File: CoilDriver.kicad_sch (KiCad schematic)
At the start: 27 parts, among them Q8 IRLML2803, Q9 SiRA99DP, U7 DRV8235RTER

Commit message: v3.1 Updates
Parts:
- removed Q9: SiRA99DP, Argus-Miscellaneous:PowerPAK SO-8, symbol Argus-IC:Q_PMOS_GDS
- removed R28, R30: 0R, Resistor_SMD:R_0603_1608Metric, symbol Device:R_Small
- added Q23: SIRA99DP-T1-GE3, Package_SO:PowerPAK_SO-8_Single, symbol Transistor_FET:Si7141DP
- C26: renamed from C11; value 10uF -> 10u; symbol Device:C -> Device:C_Small; MPN (none) -> C126617
- C27: renamed from C12; value 0.1uF -> 100n; symbol Device:C -> Device:C_Small; MPN (none) -> C307348
- C28: renamed from C13; value 1nF -> 1n; symbol Device:C -> Device:C_Small; MPN (none) -> C161231
- C29: renamed from C14; value 0.1uF -> 100n; symbol Device:C -> Device:C_Small; MPN (none) -> C307348
- D8: renamed from D3; DIS Digi-Key -> (none); DPN 1830-1064-1-ND -> (none); MFR Inolux -> (none); MPN IN-S63AT5A -> C2909774
- D9: renamed from D4; value 10V -> PTVS10VZ1USK; Field5 (none) -> 10V
- Q22: renamed from Q8; MPN (none) -> C2590
- R80: renamed from R19; value 2.7k -> 2k7; DIS Digi-Key -> (none); DPN A129693CT-ND -> (none); MFR TE -> (none); MPN CRGCQ0603F2K7 -> C237112
- R81: renamed from R22; DIS Digi-Key -> (none); DPN 311-10.0KHRCT-ND -> (none); MFR Yageo -> (none); MPN RC0603FR-0710KL -> C2479067
- R82: renamed from R23; MPN (none) -> C844931
- R83: renamed from R24; DIS Digi-Key -> (none); DPN 311-10.0KHRCT-ND -> (none); MFR Yageo -> (none); MPN RC0603FR-0710KL -> C2479067
- R84: renamed from R27; symbol Device:R -> Device:R_Small; MPN (none) -> C2479067
- R85: renamed from R33; MPN (none) -> C2484712
- R86: renamed from R29; MPN (none) -> C844915
- R87: renamed from R31; MPN (none) -> C844915
- R88: renamed from R20; MPN (none) -> C844915
- R89: renamed from R21; DNI (none) -> DNI; now not fitted; now left out of the parts list
- R90: renamed from R25; DNI (none) -> DNI; now not fitted; now left out of the parts list
- R91: renamed from R26; MPN (none) -> C844915
- R92: renamed from R32; symbol Device:R -> Device:R_Small
- R93: renamed from R34; symbol Device:R -> Device:R_Small
- R94: renamed from R35; symbol Device:R -> Device:R_Small
- renumbered F6 to F9, U7 to U8
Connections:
- net VM: now also Q23.5 (D)
- net at Q22.3 (D), R83.1: now also Q23.4 (G)
- net at F9.1, R83.2: now also Q23.1 (S), Q23.2 (S), Q23.3 (S)
- net A0_COIL renamed A0
- net A1_COIL renamed A1
- net MAIN_3V3 renamed 3V3_P
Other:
- sheet I2C Single Protection1 renamed I2C Single Protection10
- sheet I2C Single Protection2 renamed I2C Single Protection11
- note added: "#TODO: Spec Resistors"
- note added: "I2C ADDR R86, R87 +Z: 0R, 0R: 0x30 Translated: 0x10"
- company: (none) -> Carnegie Mellon University
- title: (none) -> Argus +Z Solar Panel
- moved on the sheet: C26, C27, C28, C29, D8, D9, F9, Q22, R80, R81, R82, R83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

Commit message: Local Stash
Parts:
- R87: now not fitted; now left out of the parts list
- R92: value TBD -> 560R
- R93: value TBD -> 2k7
- R94: value TBD -> 1M
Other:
- note added: "I2C ADDR R86, R87 +Z: 0R, DNP: 0x33"
- note removed: "I2C ADDR R86, R87 +Z: 0R, 0R: 0x30 Translated: 0x10"
- moved on the sheet: C29, R93, R94
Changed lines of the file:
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@@
 		)
 	)
-	(text "I2C ADDR\nR86, R87\n+Z: 0R, 0R: 0x30\nTranslated: 0x10"
+	(text "I2C ADDR\nR86, R87\n+Z: 0R, DNP: 0x33"
 		(exclude_from_sim no)
 		(at 144.526 117.856 0)
@@
 	(text "Populate after\nsetting VM\n\nStall Current = \nVREF/(R*0.0015)"
 		(exclude_from_sim no)
-		(at 182.372 144.78 0)
+		(at 182.372 144.018 0)
 		(effects
 			(font
@@
 	)
 	(junction
-		(at 226.06 135.89)
+		(at 226.06 138.43)
 		(diameter 0)
 		(color 0 0 0 0)
@@
 	(wire
 		(pts
-			(xy 209.55 135.89) (xy 209.55 138.43)
+			(xy 209.55 138.43) (xy 209.55 140.97)
 		)
 		(stroke
@@
 	(wire
 		(pts
-			(xy 226.06 133.35) (xy 226.06 135.89)
+			(xy 226.06 135.89) (xy 226.06 138.43)
 		)
 		(stroke
@@
 	(wire
 		(pts
-			(xy 226.06 135.89) (xy 240.03 135.89)
+			(xy 226.06 138.43) (xy 240.03 138.43)
 		)
 		(stroke
@@
 	(wire
 		(pts
-			(xy 209.55 143.51) (xy 209.55 146.05)
+			(xy 209.55 146.05) (xy 209.55 148.59)
 		)
 		(stroke
@@
 	(wire
 		(pts
-			(xy 209.55 135.89) (xy 226.06 135.89)
+			(xy 209.55 138.43) (xy 226.06 138.43)
 		)
 		(stroke
@@
 	(wire
 		(pts
-			(xy 226.06 135.89) (xy 226.06 138.43)
+			(xy 226.06 138.43) (xy 226.06 140.97)
 		)
 		(stroke
@@
 	(wire
 		(pts
-			(xy 226.06 143.51) (xy 226.06 146.05)
+			(xy 226.06 146.05) (xy 226.06 148.59)
 		)
 		(stroke
@@
 	(wire
 		(pts
-			(xy 226.06 125.73) (xy 226.06 128.27)
+			(xy 226.06 128.27) (xy 226.06 130.81)
 		)
 		(stroke
@@
 	)
 	(label "VREF"
-		(at 240.03 135.89 180)
+		(at 240.03 138.43 180)
 		(effects
 			(font
@@
 	(symbol
 		(lib_id "Device:R_Small")
-		(at 226.06 130.81 0)
+		(at 226.06 133.35 0)
 		(unit 1)
 		(exclude_from_sim no)
@@
 		(dnp no)
 		(property "Reference" "R93"
-			(at 227.584 129.794 0)
+			(at 227.33 132.334 0)
 			(effects
 				(font
@@
 			)
 		)
-		(property "Value" "TBD"
-			(at 227.584 132.08 0)
+		(property "Value" "2k7"
+			(at 227.33 134.62 0)
 			(effects
 				(font
@@
 		)
 		(property "Footprint" "Resistor_SMD:R_0603_1608Metric"
-			(at 226.06 130.81 0)
+			(at 226.06 133.35 0)
 			(effects
 				(font
@@
 		)
 		(property "Datasheet" "~"
-			(at 226.06 130.81 0)
+			(at 226.06 133.35 0)
 			(effects
 				(font
@@
 		)
 		(property "Description" "Resistor, small symbol"
-			(at 226.06 130.81 0)
+			(at 226.06 133.35 0)
 			(effects
 				(font
@@
 	(symbol
 		(lib_id "Device:C_Small")
-		(at 209.55 140.97 0)
+		(at 209.55 143.51 0)
 		(unit 1)
 		(exclude_from_sim no)
@@
 		(dnp no)
 		(property "Reference" "C29"
-			(at 211.836 139.954 0)
+			(at 211.836 142.494 0)
 			(effects
 				(font
@@
 		)
 		(property "Value" "100n"
-			(at 211.836 141.986 0)
+			(at 211.836 144.526 0)
 			(effects
 				(font
@@
 		)
 		(property "Footprint" "Capacitor_SMD:C_0603_1608Metric"
-			(at 209.55 140.97 0)
+			(at 209.55 143.51 0)
 			(effects
 				(font
@@
 		)
 		(property "Datasheet" "~"
-			(at 209.55 140.97 0)
+			(at 209.55 143.51 0)
 			(effects
 				(font
@@
 		)
 		(property "Description" "Unpolarized capacitor, small symbol"
-			(at 209.55 140.97 0)
+			(at 209.55 143.51 0)
 			(effects
 				(font
@@
 		)
 		(property "MPN" "C307348"
-			(at 209.55 140.97 0)
+			(at 209.55 143.51 0)
 			(effects
 				(font
@@
 	(symbol
 		(lib_id "power:GND")
-		(at 209.55 146.05 0)
+		(at 209.55 148.59 0)
 		(unit 1)
 		(exclude_from_sim no)
@@
 		(on_board yes)
 		(dnp no)
-		(fields_autoplaced yes)
 		(property "Reference" "#PWR035"
-			(at 209.55 152.4 0)
+			(at 209.55 154.94 0)
 			(effects
 				(font
@@
 		)
 		(property "Value" "GND"
-			(at 209.55 151.13 0)
+			(at 209.55 152.4 0)
 			(effects
 				(font
@@
 		)
 		(property "Footprint" ""
-			(at 209.55 146.05 0)
+			(at 209.55 148.59 0)
 			(effects
 				(font
@@
 		)
 		(property "Datasheet" ""
-			(at 209.55 146.05 0)
+			(at 209.55 148.59 0)
 			(effects
 				(font
@@
 		)
 		(property "Description" "Power symbol creates a global label with name \"GND\" , ground"
-			(at 209.55 146.05 0)
+			(at 209.55 148.59 0)
 			(effects
 				(font
@@
 	(symbol
 		(lib_id "power:GND")
-		(at 226.06 146.05 0)
+		(at 226.06 148.59 0)
 		(unit 1)
 		(exclude_from_sim no)
@@
 		(on_board yes)
 		(dnp no)
-		(fields_autoplaced yes)
 		(property "Reference" "#PWR037"
-			(at 226.06 152.4 0)
+			(at 226.06 154.94 0)
 			(effects
 				(font
@@
 		)
 		(property "Value" "GND"
-			(at 226.06 151.13 0)
+			(at 226.06 152.4 0)
 			(effects
 				(font
@@
 		)
 		(property "Footprint" ""
-			(at 226.06 146.05 0)
+			(at 226.06 148.59 0)
 			(effects
 				(font
@@
 		)
 		(property "Datasheet" ""
-			(at 226.06 146.05 0)
+			(at 226.06 148.59 0)
 			(effects
 				(font
@@
 		)
 		(property "Description" "Power symbol creates a global label with name \"GND\" , ground"
-			(at 226.06 146.05 0)
+			(at 226.06 148.59 0)
 			(effects
 				(font
@@
 	(symbol
 		(lib_id "power:+3.3V")
-		(at 226.06 125.73 0)
+		(at 226.06 128.27 0)
 		(mirror y)
 		(unit 1)
@@
 		(dnp no)
 		(property "Reference" "#SUPPLY07"
-			(at 226.06 125.73 0)
+			(at 226.06 128.27 0)
 			(effects
 				(font
@@
 		)
 		(property "Value" "3V3_P"
-			(at 226.06 121.92 0)
+			(at 226.06 124.46 0)
 			(effects
 				(font
@@
 		)
 		(property "Footprint" ""
-			(at 226.06 125.73 0)
+			(at 226.06 128.27 0)
 			(effects
 				(font
@@
 		)
 		(property "Datasheet" ""
-			(at 226.06 125.73 0)
+			(at 226.06 128.27 0)
 			(effects
 				(font
@@
 		)
 		(property "Description" "Power symbol creates a global label with name \"+3.3V\""
-			(at 226.06 125.73 0)
+			(at 226.06 128.27 0)
 			(effects
 				(font
@@
 			)
 		)
-		(property "Value" "TBD"
+		(property "Value" "560R"
 			(at 164.084 141.986 0)
 			(effects
@@
 	(symbol
 		(lib_id "Device:R_Small")
-		(at 226.06 140.97 0)
+		(at 226.06 143.51 0)
 		(unit 1)
 		(exclude_from_sim no)
@@
 		(dnp no)
 		(property "Reference" "R94"
-			(at 227.33 139.954 0)
+			(at 227.33 142.494 0)
 			(effects
 				(font
@@
 			)
 		)
-		(property "Value" "TBD"
-			(at 227.33 142.24 0)
+		(property "Value" "1M"
+			(at 227.33 144.78 0)
 			(effects
 				(font
@@
 		)
 		(property "Footprint" "Resistor_SMD:R_0603_1608Metric"
-			(at 226.06 140.97 0)
+			(at 226.06 143.51 0)
 			(effects
 				(font
@@
 		)
 		(property "Datasheet" "~"
-			(at 226.06 140.97 0)
+			(at 226.06 143.51 0)
 			(effects
 				(font
@@
 		)
 		(property "Description" "Resistor, small symbol"
-			(at 226.06 140.97 0)
+			(at 226.06 143.51 0)
 			(effects
 				(font
@@
 		(unit 1)
 		(exclude_from_sim no)
-		(in_bom yes)
+		(in_bom no)
 		(on_board yes)
-		(dnp no)
+		(dnp yes)
 		(property "Reference" "R87"
 			(at 196.342 109.728 0)

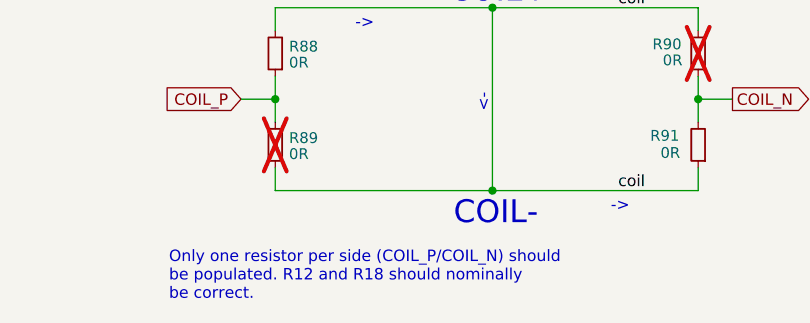
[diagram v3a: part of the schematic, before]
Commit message: Coil direction comment clarification
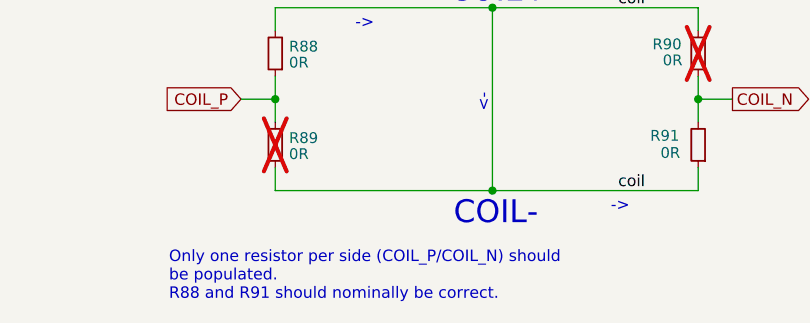
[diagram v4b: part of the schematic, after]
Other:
- note added: "Only one resistor per side (COIL_P/COIL_N) should be populated. R88 and R91 should nominally be correct."
- note removed: "Only one resistor per side (COIL_P/COIL_N) should be populated. R12 and R18 should nominally be correct."
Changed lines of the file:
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@@
 		)
 	)
-	(text "Only one resistor per side (COIL_P/COIL_N) should \nbe populated. R12 and R18 should nominally \nbe correct."
+	(text "Only one resistor per side (COIL_P/COIL_N) should \nbe populated. \nR88 and R91 should nominally be correct."
 		(exclude_from_sim no)
 		(at 42.799 171.069 0)
@@
 		)
 		(instances
-			(project "Z+"
+			(project "+Z"
 				(path "/977a45af-b6d4-4b54-8e70-e74e2c44e8e7/bc31f1ea-1b2a-44a8-9545-3b4dda72db3a"
 					(reference "C26")
@@
 		)
 		(instances
-			(project "Z+"
+			(project "+Z"
 				(path "/977a45af-b6d4-4b54-8e70-e74e2c44e8e7/bc31f1ea-1b2a-44a8-9545-3b4dda72db3a"
 					(reference "R93")
@@
 		)
 		(instances
-			(project "Z+"
+			(project "+Z"
 				(path "/977a45af-b6d4-4b54-8e70-e74e2c44e8e7/bc31f1ea-1b2a-44a8-9545-3b4dda72db3a"
 					(reference "U8")
@@
 		)
 		(instances
-			(project "Z+"
+			(project "+Z"
 				(path "/977a45af-b6d4-4b54-8e70-e74e2c44e8e7/bc31f1ea-1b2a-44a8-9545-3b4dda72db3a"
 					(reference "R80")
@@
 		)
 		(instances
-			(project "Z+"
+			(project "+Z"
 				(path "/977a45af-b6d4-4b54-8e70-e74e2c44e8e7/bc31f1ea-1b2a-44a8-9545-3b4dda72db3a"
 					(reference "#PWR031")
@@
 		)
 		(instances
-			(project "Z+"
+			(project "+Z"
 				(path "/977a45af-b6d4-4b54-8e70-e74e2c44e8e7/bc31f1ea-1b2a-44a8-9545-3b4dda72db3a"
 					(reference "#PWR034")
@@
 		)
 		(instances
-			(project "Z+"
+			(project "+Z"
 				(path "/977a45af-b6d4-4b54-8e70-e74e2c44e8e7/bc31f1ea-1b2a-44a8-9545-3b4dda72db3a"
 					(reference "#PWR023")
@@
 		)
 		(instances
-			(project "Z+"
+			(project "+Z"
 				(path "/977a45af-b6d4-4b54-8e70-e74e2c44e8e7/bc31f1ea-1b2a-44a8-9545-3b4dda72db3a"
 					(reference "#GND02")
@@
 		)
 		(instances
-			(project "Z+"
+			(project "+Z"
 				(path "/977a45af-b6d4-4b54-8e70-e74e2c44e8e7/bc31f1ea-1b2a-44a8-9545-3b4dda72db3a"
 					(reference "C29")
@@
 		)
 		(instances
-			(project "Z+"
+			(project "+Z"
 				(path "/977a45af-b6d4-4b54-8e70-e74e2c44e8e7/bc31f1ea-1b2a-44a8-9545-3b4dda72db3a"
 					(reference "#PWR035")
@@
 		)
 		(instances
-			(project "Z+"
+			(project "+Z"
 				(path "/977a45af-b6d4-4b54-8e70-e74e2c44e8e7/bc31f1ea-1b2a-44a8-9545-3b4dda72db3a"
 					(reference "#PWR037")
@@
 		)
 		(instances
-			(project "Z+"
+			(project "+Z"
 				(path "/977a45af-b6d4-4b54-8e70-e74e2c44e8e7/bc31f1ea-1b2a-44a8-9545-3b4dda72db3a"
 					(reference "D9")
@@
 		)
 		(instances
-			(project "Z+"
+			(project "+Z"
 				(path "/977a45af-b6d4-4b54-8e70-e74e2c44e8e7/bc31f1ea-1b2a-44a8-9545-3b4dda72db3a"
 					(reference "#PWR027")
@@
 		)
 		(instances
-			(project "Z+"
+			(project "+Z"
 				(path "/977a45af-b6d4-4b54-8e70-e74e2c44e8e7/bc31f1ea-1b2a-44a8-9545-3b4dda72db3a"
 					(reference "#SUPPLY07")
@@
 		)
 		(instances
-			(project "Z+"
+			(project "+Z"
 				(path "/977a45af-b6d4-4b54-8e70-e74e2c44e8e7/bc31f1ea-1b2a-44a8-9545-3b4dda72db3a"
 					(reference "#PWR030")
@@
 		)
 		(instances
-			(project "Z+"
+			(project "+Z"
 				(path "/977a45af-b6d4-4b54-8e70-e74e2c44e8e7/bc31f1ea-1b2a-44a8-9545-3b4dda72db3a"
 					(reference "R90")
@@
 		)
 		(instances
-			(project "Z+"
+			(project "+Z"
 				(path "/977a45af-b6d4-4b54-8e70-e74e2c44e8e7/bc31f1ea-1b2a-44a8-9545-3b4dda72db3a"
 					(reference "R91")
@@
 		)
 		(instances
-			(project "Z+"
+			(project "+Z"
 				(path "/977a45af-b6d4-4b54-8e70-e74e2c44e8e7/bc31f1ea-1b2a-44a8-9545-3b4dda72db3a"
 					(reference "#SUPPLY06")
@@
 		)
 		(instances
-			(project "Z+"
+			(project "+Z"
 				(path "/977a45af-b6d4-4b54-8e70-e74e2c44e8e7/bc31f1ea-1b2a-44a8-9545-3b4dda72db3a"
 					(reference "C28")
@@
 		)
 		(instances
-			(project "Z+"
+			(project "+Z"
 				(path "/977a45af-b6d4-4b54-8e70-e74e2c44e8e7/bc31f1ea-1b2a-44a8-9545-3b4dda72db3a"
 					(reference "R85")
@@
 		)
 		(instances
-			(project "Z+"
+			(project "+Z"
 				(path "/977a45af-b6d4-4b54-8e70-e74e2c44e8e7/bc31f1ea-1b2a-44a8-9545-3b4dda72db3a"
 					(reference "R84")
@@
 		)
 		(instances
-			(project "Z+"
+			(project "+Z"
 				(path "/977a45af-b6d4-4b54-8e70-e74e2c44e8e7/bc31f1ea-1b2a-44a8-9545-3b4dda72db3a"
 					(reference "#PWR029")
@@
 		)
 		(instances
-			(project "Z+"
+			(project "+Z"
 				(path "/977a45af-b6d4-4b54-8e70-e74e2c44e8e7/bc31f1ea-1b2a-44a8-9545-3b4dda72db3a"
 					(reference "R89")
@@
 		)
 		(instances
-			(project "Z+"
+			(project "+Z"
 				(path "/977a45af-b6d4-4b54-8e70-e74e2c44e8e7/bc31f1ea-1b2a-44a8-9545-3b4dda72db3a"
 					(reference "#SUPPLY05")
@@
 		)
 		(instances
-			(project "Z+"
+			(project "+Z"
 				(path "/977a45af-b6d4-4b54-8e70-e74e2c44e8e7/bc31f1ea-1b2a-44a8-9545-3b4dda72db3a"
 					(reference "R92")
@@
 		)
 		(instances
-			(project "Z+"
+			(project "+Z"
 				(path "/977a45af-b6d4-4b54-8e70-e74e2c44e8e7/bc31f1ea-1b2a-44a8-9545-3b4dda72db3a"
 					(reference "D8")
@@
 		)
 		(instances
-			(project "Z+"
+			(project "+Z"
 				(path "/977a45af-b6d4-4b54-8e70-e74e2c44e8e7/bc31f1ea-1b2a-44a8-9545-3b4dda72db3a"
 					(reference "#GND01")
@@
 		)
 		(instances
-			(project "Z+"
+			(project "+Z"
 				(path "/977a45af-b6d4-4b54-8e70-e74e2c44e8e7/bc31f1ea-1b2a-44a8-9545-3b4dda72db3a"
 					(reference "R86")
@@
 		)
 		(instances
-			(project "Z+"
+			(project "+Z"
 				(path "/977a45af-b6d4-4b54-8e70-e74e2c44e8e7/bc31f1ea-1b2a-44a8-9545-3b4dda72db3a"
 					(reference "R82")
@@
 		)
 		(instances
-			(project "Z+"
+			(project "+Z"
 				(path "/977a45af-b6d4-4b54-8e70-e74e2c44e8e7/bc31f1ea-1b2a-44a8-9545-3b4dda72db3a"
 					(reference "R94")
@@
 		)
 		(instances
-			(project "Z+"
+			(project "+Z"
 				(path "/977a45af-b6d4-4b54-8e70-e74e2c44e8e7/bc31f1ea-1b2a-44a8-9545-3b4dda72db3a"
 					(reference "R87")
@@
 		)
 		(instances
-			(project "Z+"
+			(project "+Z"
 				(path "/977a45af-b6d4-4b54-8e70-e74e2c44e8e7/bc31f1ea-1b2a-44a8-9545-3b4dda72db3a"
 					(reference "R88")
@@
 		)
 		(instances
-			(project "Z+"
+			(project "+Z"
 				(path "/977a45af-b6d4-4b54-8e70-e74e2c44e8e7/bc31f1ea-1b2a-44a8-9545-3b4dda72db3a"
 					(reference "#PWR022")
@@
 		)
 		(instances
-			(project "Z+"
+			(project "+Z"
 				(path "/977a45af-b6d4-4b54-8e70-e74e2c44e8e7/bc31f1ea-1b2a-44a8-9545-3b4dda72db3a"
 					(reference "#PWR025")
@@
 		)
 		(instances
-			(project "Z+"
+			(project "+Z"
 				(path "/977a45af-b6d4-4b54-8e70-e74e2c44e8e7/bc31f1ea-1b2a-44a8-9545-3b4dda72db3a"
 					(reference "Q22")
@@
 		)
 		(instances
-			(project "Z+"
+			(project "+Z"
 				(path "/977a45af-b6d4-4b54-8e70-e74e2c44e8e7/bc31f1ea-1b2a-44a8-9545-3b4dda72db3a"
 					(reference "R81")
@@
 		)
 		(instances
-			(project "Z+"
+			(project "+Z"
 				(path "/977a45af-b6d4-4b54-8e70-e74e2c44e8e7/bc31f1ea-1b2a-44a8-9545-3b4dda72db3a"
 					(reference "C27")
@@
 		)
 		(instances
-			(project "Z+"
+			(project "+Z"
 				(path "/977a45af-b6d4-4b54-8e70-e74e2c44e8e7/bc31f1ea-1b2a-44a8-9545-3b4dda72db3a"
 					(reference "#SUPPLY04")
@@
 		)
 		(instances
-			(project "Z+"
+			(project "+Z"
 				(path "/977a45af-b6d4-4b54-8e70-e74e2c44e8e7/bc31f1ea-1b2a-44a8-9545-3b4dda72db3a"
 					(reference "F9")
@@
 		)
 		(instances
-			(project "Z+"
+			(project "+Z"
 				(path "/977a45af-b6d4-4b54-8e70-e74e2c44e8e7/bc31f1ea-1b2a-44a8-9545-3b4dda72db3a"
 					(reference "R83")
